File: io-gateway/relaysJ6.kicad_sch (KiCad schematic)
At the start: 20 parts, among them U1 SN65LBC176QDR, U2 TPS76350, U4 ISO7741, U5 SN6501DBVR

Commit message: upd
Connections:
- net +5V: no longer C1.1, C12.1, C6.1, TR1.2, U5.2 (VCC)
- net +5VP renamed +3.3VA
- new net +3V3: C1.1, C12.1, C6.1, TR1.2, U5.2 (VCC)
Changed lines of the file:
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@@
 	(wire
 		(pts
-			(xy 68.58 46.99) (xy 68.58 49.53)
+			(xy 68.58 45.72) (xy 68.58 49.53)
 		)
 		(stroke
@@
 	(wire
 		(pts
-			(xy 209.55 86.36) (xy 209.55 88.9)
+			(xy 209.55 83.82) (xy 209.55 88.9)
 		)
 		(stroke
@@
 	)
 	(symbol
+		(lib_id "power:+3V3")
+		(at 68.58 45.72 0)
+		(unit 1)
+		(exclude_from_sim no)
+		(in_bom yes)
+		(on_board yes)
+		(dnp no)
+		(fields_autoplaced yes)
+		(property "Reference" "#PWR060"
+			(at 68.58 49.53 0)
+			(effects
+				(font
+					(size 1.27 1.27)
+				)
+				(hide yes)
+			)
+		)
+		(property "Value" "+3V3"
+			(at 68.58 40.64 0)
+			(effects
+				(font
+					(size 1.27 1.27)
+				)
+			)
+		)
+		(property "Footprint" ""
+			(at 68.58 45.72 0)
+			(effects
+				(font
+					(size 1.27 1.27)
+				)
+				(hide yes)
+			)
+		)
+		(property "Datasheet" ""
+			(at 68.58 45.72 0)
+			(effects
+				(font
+					(size 1.27 1.27)
+				)
+				(hide yes)
+			)
+		)
+		(property "Description" "Power symbol creates a global label with name \"+3V3\""
+			(at 68.58 45.72 0)
+			(effects
+				(font
+					(size 1.27 1.27)
+				)
+				(hide yes)
+			)
+		)
+		(pin "1"
+		)
+		(instances
+			(project ""
+				(path "/2cb6f94b-272a-4ed7-b08d-c3630bda6156/1308d9d5-cfd2-45e8-87f7-78f75fc0ae30"
+					(reference "#PWR060")
+					(unit 1)
+				)
+			)
+		)
+	)
+	(symbol
 		(lib_id "Device:R")
 		(at 148.59 101.6 0)
@@
 				(path "/2cb6f94b-272a-4ed7-b08d-c3630bda6156/1308d9d5-cfd2-45e8-87f7-78f75fc0ae30"
 					(reference "R2")
+					(unit 1)
+				)
+			)
+		)
+	)
+	(symbol
+		(lib_id "power:+3.3VA")
+		(at 209.55 83.82 0)
+		(unit 1)
+		(exclude_from_sim no)
+		(in_bom yes)
+		(on_board yes)
+		(dnp no)
+		(fields_autoplaced yes)
+		(property "Reference" "#PWR070"
+			(at 209.55 87.63 0)
+			(effects
+				(font
+					(size 1.27 1.27)
+				)
+				(hide yes)
+			)
+		)
+		(property "Value" "+3.3VA"
+			(at 209.55 78.74 0)
+			(effects
+				(font
+					(size 1.27 1.27)
+				)
+			)
+		)
+		(property "Footprint" ""
+			(at 209.55 83.82 0)
+			(effects
+				(font
+					(size 1.27 1.27)
+				)
+				(hide yes)
+			)
+		)
+		(property "Datasheet" ""
+			(at 209.55 83.82 0)
+			(effects
+				(font
+					(size 1.27 1.27)
+				)
+				(hide yes)
+			)
+		)
+		(property "Description" "Power symbol creates a global label with name \"+3.3VA\""
+			(at 209.55 83.82 0)
+			(effects
+				(font
+					(size 1.27 1.27)
+				)
+				(hide yes)
+			)
+		)
+		(pin "1"
+		)
+		(instances
+			(project ""
+				(path "/2cb6f94b-272a-4ed7-b08d-c3630bda6156/1308d9d5-cfd2-45e8-87f7-78f75fc0ae30"
+					(reference "#PWR070")
 					(unit 1)
 				)
@@
 	)
 	(symbol
-		(lib_id "power:+5VP")
-		(at 209.55 86.36 0)
-		(unit 1)
-		(exclude_from_sim no)
-		(in_bom yes)
-		(on_board yes)
-		(dnp no)
-		(fields_autoplaced yes)
-		(property "Reference" "#PWR070"
-			(at 209.55 90.17 0)
-			(effects
-				(font
-					(size 1.27 1.27)
-				)
-				(hide yes)
-			)
-		)
-		(property "Value" "+5VP"
-			(at 209.55 81.28 0)
-			(effects
-				(font
-					(size 1.27 1.27)
-				)
-			)
-		)
-		(property "Footprint" ""
-			(at 209.55 86.36 0)
-			(effects
-				(font
-					(size 1.27 1.27)
-				)
-				(hide yes)
-			)
-		)
-		(property "Datasheet" ""
-			(at 209.55 86.36 0)
-			(effects
-				(font
-					(size 1.27 1.27)
-				)
-				(hide yes)
-			)
-		)
-		(property "Description" "Power symbol creates a global label with name \"+5VP\""
-			(at 209.55 86.36 0)
-			(effects
-				(font
-					(size 1.27 1.27)
-				)
-				(hide yes)
-			)
-		)
-		(pin "1"
-		)
-		(instances
-			(project ""
-				(path "/2cb6f94b-272a-4ed7-b08d-c3630bda6156/1308d9d5-cfd2-45e8-87f7-78f75fc0ae30"
-					(reference "#PWR070")
-					(unit 1)
-				)
-			)
-		)
-	)
-	(symbol
 		(lib_id "PowerManagement:SN6501DBVR")
 		(at 57.15 83.82 0)
@@
 					(unit 1)
 				)
-			)
-		)
-	)
-	(symbol
-		(lib_id "power:+5V")
-		(at 68.58 46.99 0)
-		(unit 1)
-		(exclude_from_sim no)
-		(in_bom yes)
-		(on_board yes)
-		(dnp no)
-		(fields_autoplaced yes)
-		(property "Reference" "#PWR060"
-			(at 68.58 50.8 0)
-			(effects
-				(font
-					(size 1.27 1.27)
-				)
-				(hide yes)
-			)
-		)
-		(property "Value" "+5V"
-			(at 68.58 41.91 0)
-			(effects
-				(font
-					(size 1.27 1.27)
-				)
-			)
-		)
-		(property "Footprint" ""
-			(at 68.58 46.99 0)
-			(effects
-				(font
-					(size 1.27 1.27)
-				)
-				(hide yes)
-			)
-		)
-		(property "Datasheet" ""
-			(at 68.58 46.99 0)
-			(effects
-				(font
-					(size 1.27 1.27)
-				)
-				(hide yes)
-			)
-		)
-		(property "Description" "Power symbol creates a global label with name \"+5V\""
-			(at 68.58 46.99 0)
-			(effects
-				(font
-					(size 1.27 1.27)
-				)
-				(hide yes)
-			)
-		)
-		(pin "1"
-		)
-		(instances
-			(project "io-gateway"
-				(path "/2cb6f94b-272a-4ed7-b08d-c3630bda6156/1308d9d5-cfd2-45e8-87f7-78f75fc0ae30"
-					(reference "#PWR060")
-					(unit 1)
-				)

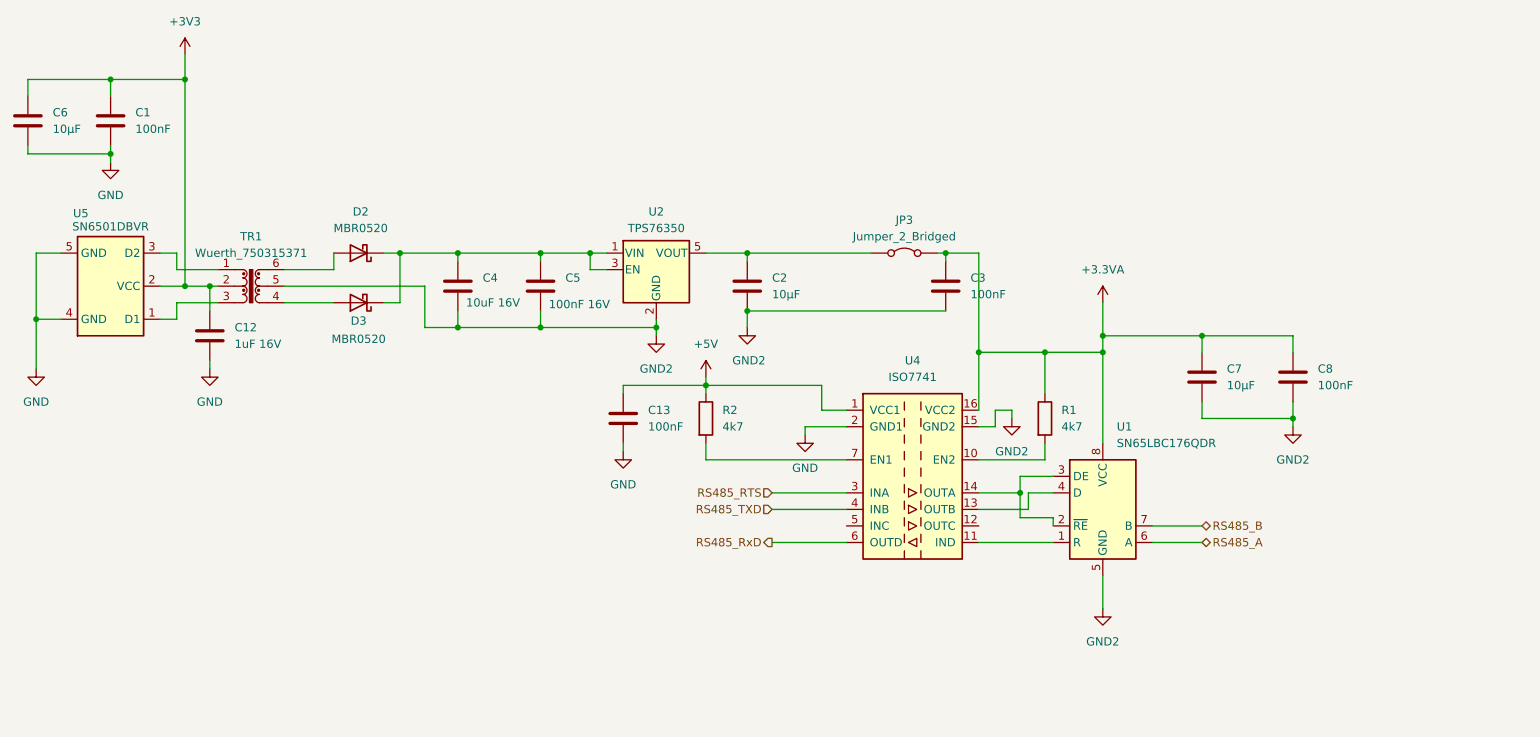
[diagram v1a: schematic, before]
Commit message: Add ESD protection for RS485
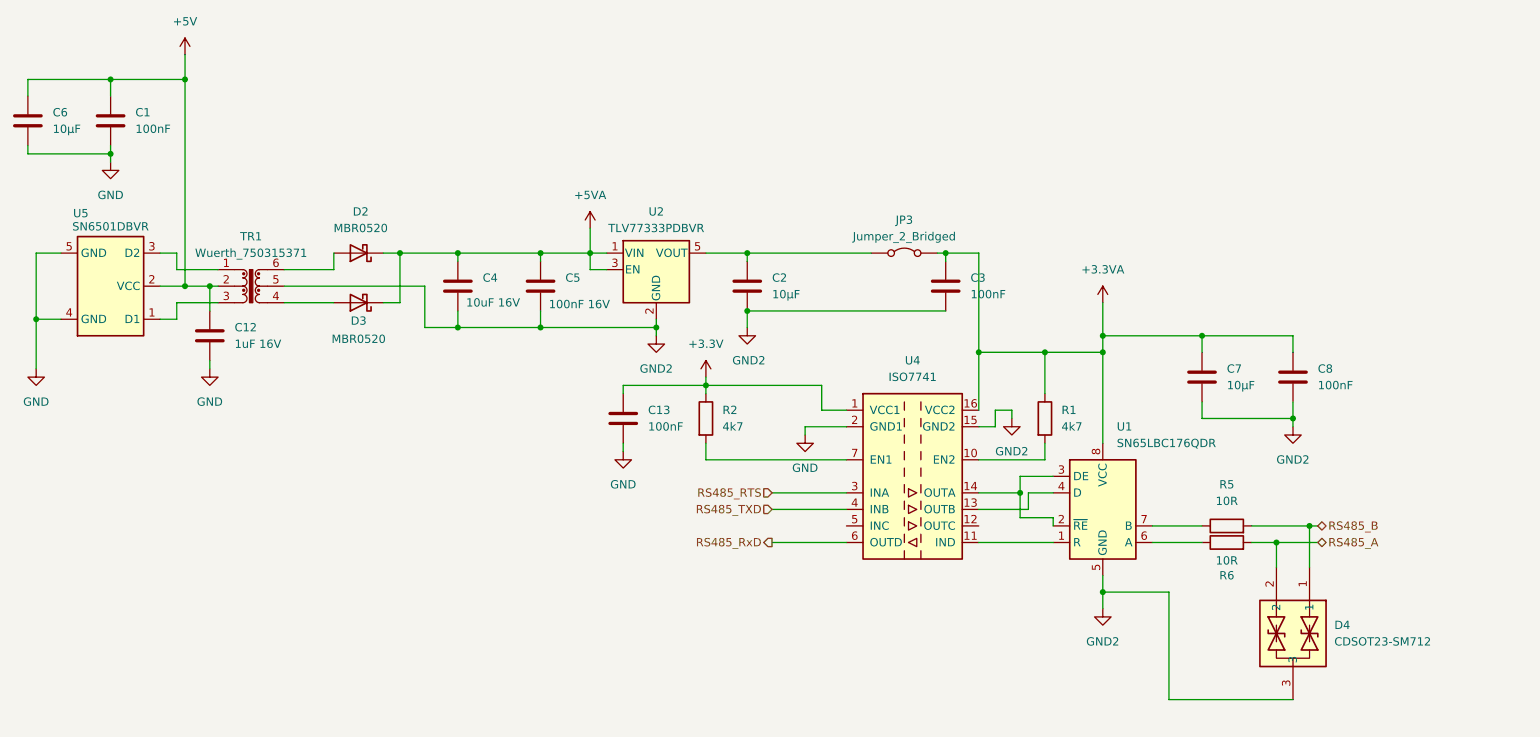
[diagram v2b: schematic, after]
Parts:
- added D4: CDSOT23-SM712, TVS:SOT95P230X117-3N, symbol CDSOT23-SM712:CDSOT23-SM712
- added R5, R6: 10R, Resistor_SMD:R_0603_1608Metric_Pad0.98x0.95mm_HandSolder, symbol Device:R
- U2: value TPS76350 -> TLV77333PDBVR
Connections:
- net +3V3 is gone; now on net +5V: C1.1, C12.1, C6.1, TR1.2, U5.2 (VCC)
- net +5V: no longer C13.1, R2.1, U4.1 (VCC1)
- net GND2: now also D4.3
- net RS485_A: now also D4.2, R6.2; no longer U1.6 (A)
- net RS485_B: now also D4.1, R5.2; no longer U1.7 (B)
- net +5VA: now reaches C4.1, C5.1, D2.1 (K), D3.1 (K), U2.1 (VIN), U2.3 (EN)
- new net: R6.1, U1.6 (A)
- new net: R5.1, U1.7 (B)
- new net +3.3V: C13.1, R2.1, U4.1 (VCC1)

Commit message: upd
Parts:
- added R7: NM, Resistor_SMD:R_0603_1608Metric_Pad0.98x0.95mm_HandSolder, symbol Device:R
- added RT1: 120R NM, Resistor_SMD:R_0603_1608Metric_Pad0.98x0.95mm_HandSolder, symbol Device:R
- U1: value SN65LBC176QDR -> SN65HVD7
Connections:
- net +3.3V: now also R7.2
- net RS485_A: now also D4.1, RT1.2; no longer D4.2
- net RS485_B: now also D4.2, RT1.1; no longer D4.1
- net RS485_RxD: now also R7.1
- net RS485_TXD: now also U4.5 (INC); no longer U4.4 (INB)
- net at U1.2 (~{RE}), U4.14 (OUTA): no longer U1.3 (DE)
- net at U4.13 (OUTB): now also U1.3 (DE); no longer U1.4 (D)
- net at U4.12 (OUTC): now also U1.4 (D)
- net RS485_RTS renamed RS485_nRE
- new net RS485_DE: U4.4 (INB)
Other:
- moved on the sheet: D4

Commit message: V1.2
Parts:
- RT1: value 120R NM -> DNP
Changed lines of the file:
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@@
 			)
 		)
-		(property "Value" "120R NM"
+		(property "Value" "DNP"
 			(at 242.57 121.9199 0)
 			(effects
